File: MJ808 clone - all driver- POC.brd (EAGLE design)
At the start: 35.5 x 35.5 mm, 38 parts, among them IC1 ATTINY4313-MMH, IC2 PRQV8.00CR1510Y00L, IC6 MCP2515, IC7 MAX16820, IC8 MCP2561-2, IC9 TPS709-Q1, K1 CRTL, Q1 PMV213SN,215, X1 22-23-2021, X2 22-23-2021

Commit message: - updated values for LED1 and LED2, re-generated gerbers
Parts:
- LED1: value XMLBWT-00-0000-0000U20E2 -> LTST-C281KRKT
- LED2: value XMLBWT-00-0000-0000U20E2 -> LTST-C281KGKT
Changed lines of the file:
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@@
 <attribute name="VALUE" x="14.405" y="7.885" size="1.27" layer="28" rot="MR270"/>
 </element>
-<element name="LED1" library="led" library_urn="urn:adsk.eagle:library:259" package="CHIP-LED0805" package3d_urn="urn:adsk.eagle:package:15818/1" value="XMLBWT-00-0000-0000U20E2 " x="10.25" y="7.25" smashed="yes">
+<element name="LED1" library="led" library_urn="urn:adsk.eagle:library:259" package="CHIP-LED0805" package3d_urn="urn:adsk.eagle:package:15818/1" value="LTST-C281KRKT" x="10.25" y="7.25" smashed="yes">
 <attribute name="NAME" x="8.75" y="7.25" size="1" layer="25" font="vector" rot="R90" align="center"/>
 <attribute name="VALUE" x="12.79" y="5.98" size="1.27" layer="27" rot="R90"/>
 </element>
-<element name="LED2" library="led" library_urn="urn:adsk.eagle:library:259" package="CHIP-LED0805" package3d_urn="urn:adsk.eagle:package:15818/1" value="XMLBWT-00-0000-0000U20E2 " x="18.75" y="7.25" smashed="yes">
+<element name="LED2" library="led" library_urn="urn:adsk.eagle:library:259" package="CHIP-LED0805" package3d_urn="urn:adsk.eagle:package:15818/1" value="LTST-C281KGKT" x="18.75" y="7.25" smashed="yes">
 <attribute name="NAME" x="20.25" y="7.5" size="1" layer="25" font="vector" rot="R90" align="center"/>
 <attribute name="VALUE" x="21.29" y="5.98" size="1.27" layer="27" rot="R90"/>

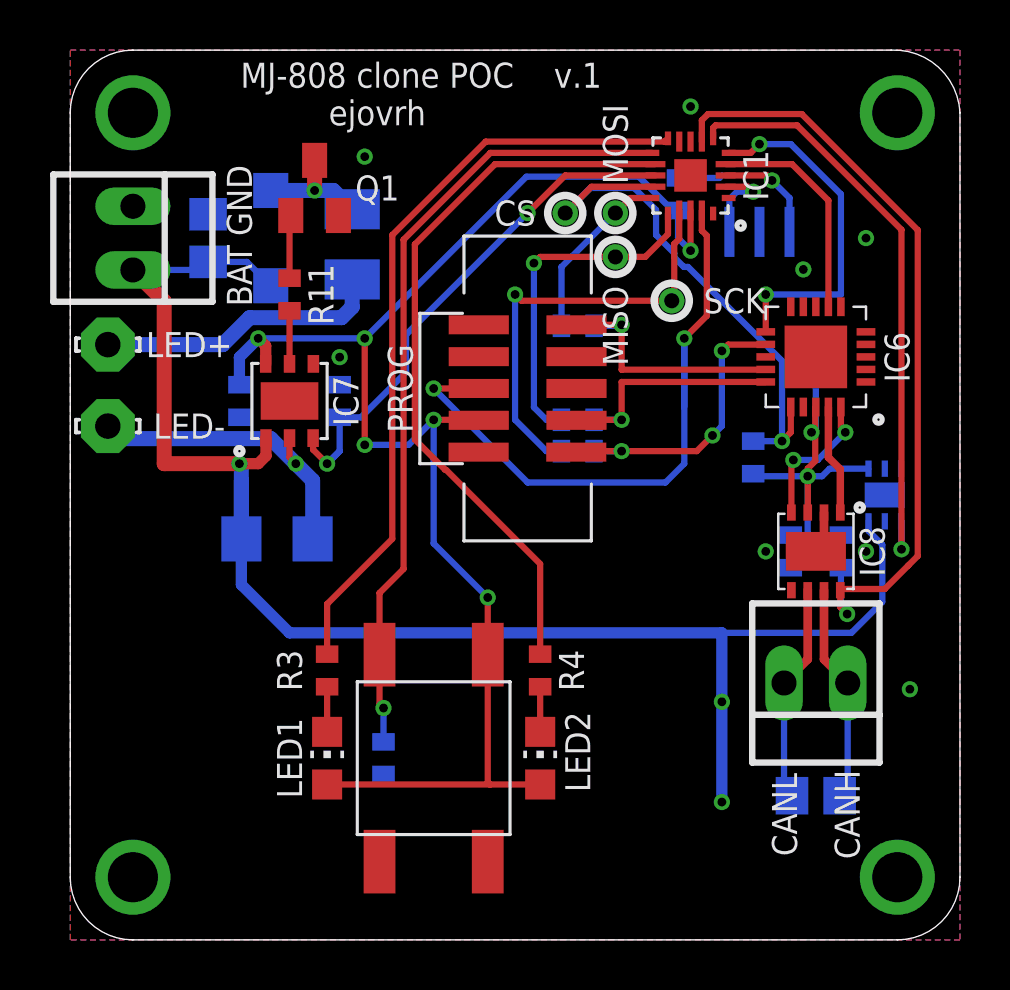
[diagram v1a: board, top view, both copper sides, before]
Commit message: - added copper edge
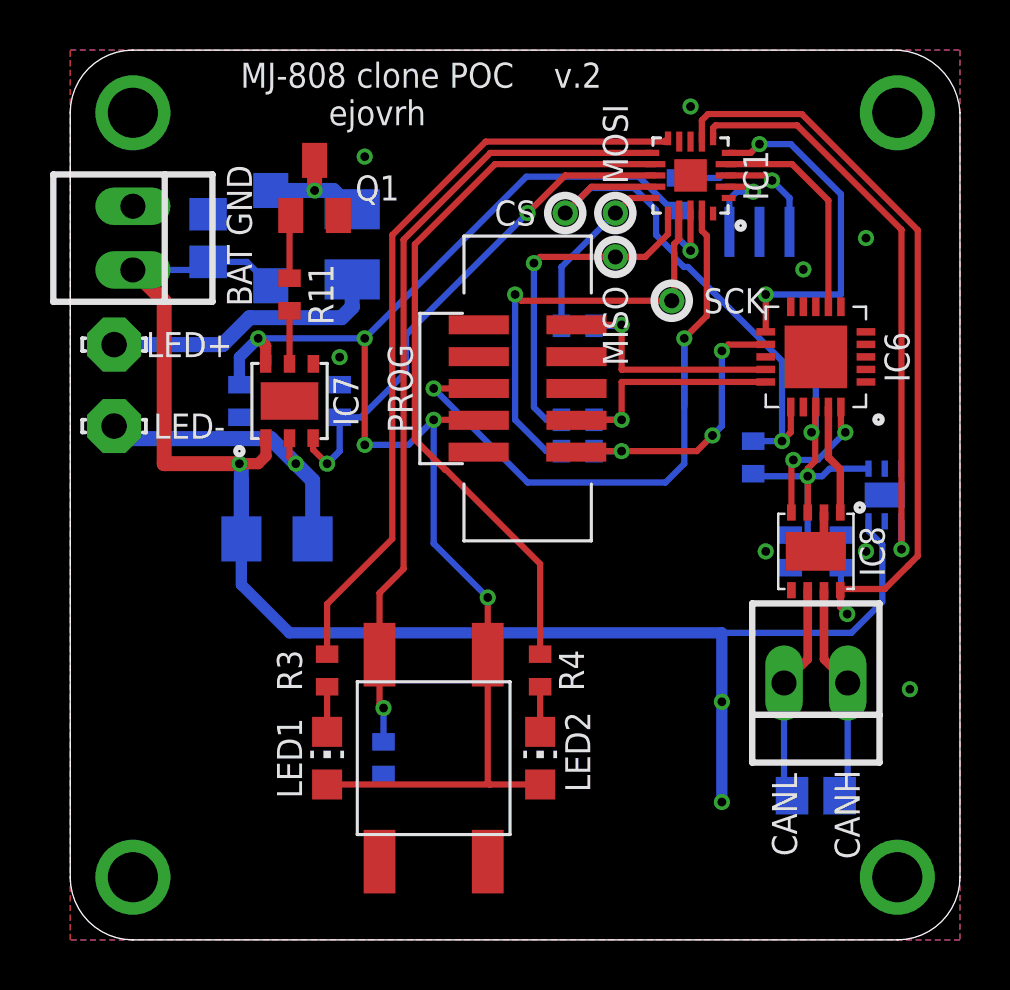
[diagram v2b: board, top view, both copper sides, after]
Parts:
- moved LSP1 0.25 mm to (1.75, 20.5)
- moved LSP2 0.25 mm to (1.75, 23.8)
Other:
- board text added: "v.2"
- board text removed: "v.1"
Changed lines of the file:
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@@
 <?xml version="1.0" encoding="utf-8"?>
 <!DOCTYPE eagle SYSTEM "eagle.dtd">
-<eagle version="8.5.0">
+<eagle version="8.6.1">
 <drawing>
 <settings>
@@
 <wire x1="33" y1="0" x2="35.5" y2="2.5" width="0" layer="20" curve="90"/>
 <wire x1="0" y1="2.5" x2="2.5" y2="0" width="0" layer="20" curve="90"/>
-<text x="20.25" y="34.5" size="1" layer="21" font="vector" align="center">v.1</text>
+<text x="20.25" y="34.5" size="1" layer="21" font="vector" align="center">v.2</text>
 <text x="31" y="5" size="1" layer="25" font="vector" rot="R90" align="center">CANH</text>
 <text x="28.5" y="5" size="1" layer="25" font="vector" rot="R90" align="center">CANL</text>
@@
 </class>
 </classes>
-<designrules name="markovac_2layer *">
+<designrules name="markovac_2layer">
 <description language="hr">&lt;b&gt;EAGLE Design Rules&lt;/b&gt;
 &lt;p&gt;
@@
 <param name="mdViaViaSameLayer" value="8mil"/>
 <param name="mnLayersViaInSmd" value="2"/>
-<param name="mdCopperDimension" value="0mil"/>
+<param name="mdCopperDimension" value="0.5mm"/>
 <param name="mdDrill" value="8mil"/>
 <param name="mdSmdStop" value="0mil"/>
 <param name="msWidth" value="0.2mm"/>
-<param name="msDrill" value="0.3mm"/>
+<param name="msDrill" value="0.35mm"/>
 <param name="msMicroVia" value="0.25mm"/>
 <param name="msBlindViaRatio" value="0.5"/>
@@
 <param name="mlMinCreamFrame" value="0mil"/>
 <param name="mlMaxCreamFrame" value="0mil"/>
-<param name="mlViaStopLimit" value="25mil"/>
+<param name="mlViaStopLimit" value="0.35mm"/>
 <param name="srRoundness" value="0"/>
 <param name="srMinRoundness" value="0mil"/>
@@
 <param name="dpMaxLengthDifference" value="10mm"/>
 <param name="dpGapFactor" value="2.5"/>
-<param name="checkAngle" value="0"/>
-<param name="checkFont" value="1"/>
+<param name="checkAngle" value="1"/>
+<param name="checkFont" value="0"/>
 <param name="checkRestrict" value="1"/>
 <param name="checkStop" value="0"/>
@@
 <attribute name="SPICEPREFIX" value="L" x="11.25" y="27.75" size="1.778" layer="28" rot="MR270" display="off"/>
 </element>
-<element name="LSP1" library="solpad" library_urn="urn:adsk.eagle:library:364" package="LSP10" package3d_urn="urn:adsk.eagle:package:26501/1" value="LSP10" x="1.5" y="20.5" smashed="yes">
-<attribute name="VALUE" x="1.5" y="20.754" size="0.0254" layer="27"/>
-</element>
-<element name="LSP2" library="solpad" library_urn="urn:adsk.eagle:library:364" package="LSP10" package3d_urn="urn:adsk.eagle:package:26501/1" value="LSP10" x="1.5" y="23.75" smashed="yes">
-<attribute name="VALUE" x="1.5" y="24.004" size="0.0254" layer="27"/>
+<element name="LSP1" library="solpad" library_urn="urn:adsk.eagle:library:364" package="LSP10" package3d_urn="urn:adsk.eagle:package:26501/1" value="LSP10" x="1.75" y="20.5" smashed="yes">
+<attribute name="VALUE" x="1.75" y="20.754" size="0.0254" layer="27"/>
+</element>
+<element name="LSP2" library="solpad" library_urn="urn:adsk.eagle:library:364" package="LSP10" package3d_urn="urn:adsk.eagle:package:26501/1" value="LSP10" x="1.75" y="23.75" smashed="yes">
+<attribute name="VALUE" x="1.75" y="24.004" size="0.0254" layer="27"/>
 </element>
 <element name="Q1" library="adafruit" library_urn="urn:adsk.eagle:library:420" package="SOT23" value="PMV213SN,215" x="9.75" y="30" smashed="yes">
@@
 <via x="9" y="19" extent="1-16" drill="0.35"/>
 <wire x1="8" y1="20" x2="9" y2="19" width="0.6" layer="16"/>
-<wire x1="1.5" y1="20.5" x2="2" y2="20" width="0.6" layer="16"/>
-<wire x1="2" y1="20" x2="8" y2="20" width="0.6" layer="16"/>
+<wire x1="1.75" y1="20.5" x2="2.25" y2="20" width="0.6" layer="16"/>
+<wire x1="2.25" y1="20" x2="8" y2="20" width="0.6" layer="16"/>
 <wire x1="9" y1="19" x2="9.672" y2="18.328" width="0.6" layer="16"/>
 <wire x1="9.672" y1="18.328" x2="9.672" y2="16" width="0.6" layer="16"/>
@@
 <contactref element="L1" pad="2"/>
 <contactref element="LSP2" pad="MP"/>
-<wire x1="1.5" y1="23.75" x2="6.08326875" y2="23.75" width="0.6" layer="16"/>
+<wire x1="1.75" y1="23.75" x2="6.08326875" y2="23.75" width="0.6" layer="16"/>
 <wire x1="6.08326875" y1="23.75" x2="7.15826875" y2="24.825" width="0.6" layer="16"/>
 <wire x1="10.825" y1="24.825" x2="7.15826875" y2="24.825" width="0.6" layer="16"/>

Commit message: - sized down ground plane of ICs to make soldering easier - corrected tname and bname positions
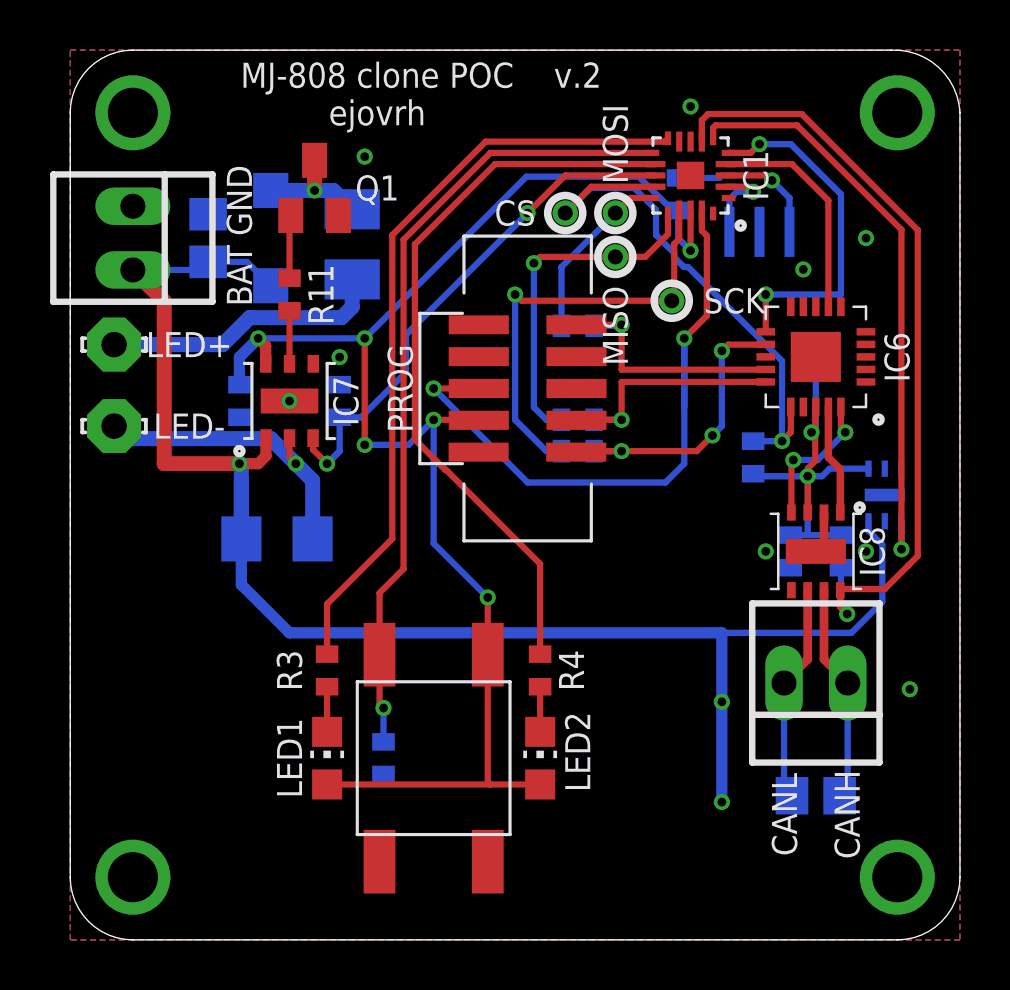
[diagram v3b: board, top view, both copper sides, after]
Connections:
- net GND: no longer IC6.GND1
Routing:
- net GND: vias 12 -> 13
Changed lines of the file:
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@@
 <grid distance="0.25" unitdist="mm" unit="mm" style="dots" multiple="1" display="yes" altdistance="0.01" altunitdist="mm" altunit="mm"/>
 <layers>
-<layer number="1" name="Top" color="4" fill="1" visible="yes" active="yes"/>
+<layer number="1" name="Top" color="4" fill="1" visible="no" active="yes"/>
 <layer number="2" name="Route2" color="1" fill="3" visible="no" active="no"/>
 <layer number="3" name="Route3" color="4" fill="3" visible="no" active="no"/>
@@
 <layer number="19" name="Unrouted" color="6" fill="1" visible="yes" active="yes"/>
 <layer number="20" name="Dimension" color="24" fill="1" visible="yes" active="yes"/>
-<layer number="21" name="tPlace" color="7" fill="1" visible="yes" active="yes"/>
+<layer number="21" name="tPlace" color="7" fill="1" visible="no" active="yes"/>
 <layer number="22" name="bPlace" color="7" fill="1" visible="yes" active="yes"/>
-<layer number="23" name="tOrigins" color="15" fill="1" visible="yes" active="yes"/>
+<layer number="23" name="tOrigins" color="15" fill="1" visible="no" active="yes"/>
 <layer number="24" name="bOrigins" color="15" fill="1" visible="yes" active="yes"/>
 <layer number="25" name="tNames" color="7" fill="1" visible="no" active="yes"/>
-<layer number="26" name="bNames" color="7" fill="1" visible="no" active="yes"/>
+<layer number="26" name="bNames" color="7" fill="1" visible="yes" active="yes"/>
 <layer number="27" name="tValues" color="7" fill="1" visible="no" active="yes"/>
 <layer number="28" name="bValues" color="7" fill="1" visible="no" active="yes"/>
@@
 <layer number="37" name="tTest" color="7" fill="1" visible="no" active="yes"/>
 <layer number="38" name="bTest" color="7" fill="1" visible="no" active="yes"/>
-<layer number="39" name="tKeepout" color="4" fill="11" visible="yes" active="yes"/>
+<layer number="39" name="tKeepout" color="4" fill="11" visible="no" active="yes"/>
 <layer number="40" name="bKeepout" color="1" fill="11" visible="yes" active="yes"/>
-<layer number="41" name="tRestrict" color="4" fill="10" visible="yes" active="yes"/>
+<layer number="41" name="tRestrict" color="4" fill="10" visible="no" active="yes"/>
 <layer number="42" name="bRestrict" color="1" fill="10" visible="yes" active="yes"/>
-<layer number="43" name="vRestrict" color="2" fill="10" visible="yes" active="yes"/>
+<layer number="43" name="vRestrict" color="2" fill="10" visible="no" active="yes"/>
 <layer number="44" name="Drills" color="7" fill="1" visible="yes" active="yes"/>
 <layer number="45" name="Holes" color="7" fill="1" visible="yes" active="yes"/>
@@
 <layer number="49" name="Reference" color="7" fill="1" visible="no" active="yes"/>
 <layer number="50" name="dxf" color="7" fill="1" visible="no" active="no"/>
-<layer number="51" name="tDocu" color="7" fill="1" visible="yes" active="yes"/>
+<layer number="51" name="tDocu" color="7" fill="1" visible="no" active="yes"/>
 <layer number="52" name="bDocu" color="7" fill="1" visible="yes" active="yes"/>
 <layer number="53" name="tGND_GNDA" color="7" fill="9" visible="no" active="no"/>
@@
 </element>
 <element name="R10" library="rcl" library_urn="urn:adsk.eagle:library:334" package="R1206" package3d_urn="urn:adsk.eagle:package:23540/2" value="0.25 / 2W" x="8.25" y="16" smashed="yes" rot="MR0">
-<attribute name="NAME" x="8.25" y="13" size="1" layer="26" font="vector" rot="MR0" align="center"/>
+<attribute name="NAME" x="8.25" y="14.25" size="1" layer="26" font="vector" rot="MR0" align="center"/>
 <attribute name="VALUE" x="8.885" y="13.46" size="1.27" layer="28" rot="MR0"/>
 </element>
@@
 </element>
 <element name="IC2" library="PRQV8.00CR1510Y00L - 8MHz resonator" package="SMT" value=" PRQV8.00CR1510Y00L" x="27.5" y="28.25" smashed="yes" rot="MR0">
-<attribute name="NAME" x="30.45" y="28.25" size="1" layer="26" font="vector" rot="MR90" align="center"/>
+<attribute name="NAME" x="30.2" y="28.25" size="1" layer="26" font="vector" rot="MR90" align="center"/>
 </element>
 <element name="PROG" library="SPI 1.27mm 10pin header" package="SMT-JTAG" value="SPI-1.27-10-PIN-HEADER" x="18.25" y="22" smashed="yes" rot="R90">
@@
 </element>
 <element name="R9" library="rcl" library_urn="urn:adsk.eagle:library:334" package="R0402" package3d_urn="urn:adsk.eagle:package:23547/1" value="330" x="20.25" y="20.75" smashed="yes" rot="MR0">
-<attribute name="NAME" x="20.25" y="24.5" size="1" layer="26" font="vector" rot="MR0" align="center"/>
+<attribute name="NAME" x="20.25" y="22" size="1" layer="26" font="vector" rot="MR0" align="center"/>
 <attribute name="VALUE" x="20.885" y="18.845" size="1.27" layer="28" rot="MR0"/>
 </element>
 <element name="R8" library="rcl" library_urn="urn:adsk.eagle:library:334" package="R0402" package3d_urn="urn:adsk.eagle:package:23547/1" value="330" x="20.25" y="24.5" smashed="yes" rot="MR0">
-<attribute name="NAME" x="20.25" y="28.25" size="1" layer="26" font="vector" rot="MR0" align="center"/>
+<attribute name="NAME" x="20.25" y="25.75" size="1" layer="26" font="vector" rot="MR0" align="center"/>
 <attribute name="VALUE" x="20.885" y="22.595" size="1.27" layer="28" rot="MR0"/>
 </element>
 <element name="R6" library="rcl" library_urn="urn:adsk.eagle:library:334" package="R0402" package3d_urn="urn:adsk.eagle:package:23547/1" value="330" x="20.25" y="19.5" smashed="yes" rot="MR0">
-<attribute name="NAME" x="20.25" y="23.25" size="1" layer="26" font="vector" rot="MR0" align="center"/>
+<attribute name="NAME" x="20.25" y="18.25" size="1" layer="26" font="vector" rot="MR0" align="center"/>
 <attribute name="VALUE" x="20.885" y="17.595" size="1.27" layer="28" rot="MR0"/>
 </element>
 <element name="R12" library="rcl" library_urn="urn:adsk.eagle:library:334" package="R0402" package3d_urn="urn:adsk.eagle:package:23547/1" value="10k" x="30.75" y="15.5" smashed="yes" rot="MR270">
-<attribute name="NAME" x="32" y="15.5" size="1" layer="26" rot="MR270" align="center"/>
+<attribute name="NAME" x="32" y="13.25" size="1" layer="26" rot="MR270" align="center"/>
 <attribute name="VALUE" x="32.655" y="16.135" size="1.27" layer="28" rot="MR270"/>
 </element>
@@
 <contactref element="Q1" pad="2"/>
 <contactref element="IC6" pad="GND"/>
-<contactref element="IC6" pad="GND1"/>
 <contactref element="IC6" pad="GND6"/>
 <contactref element="IC8" pad="GND"/>
@@
 <wire x1="25.9" y1="30.4" x2="26" y2="30.5" width="0.25" layer="16"/>
 <contactref element="R1" pad="2"/>
+<via x="8.75" y="21.5" extent="1-16" drill="0.35"/>
+<wire x1="29.75" y1="23.9" x2="29.75" y2="23.26" width="0" layer="19" extent="1-16"/>
+<wire x1="29.75" y1="15.5" x2="28.75" y2="14.85" width="0" layer="19" extent="1-16"/>
 </signal>
 <signal name="DIM_FRONT">

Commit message: - added pulldown on 5V LDO enable pin
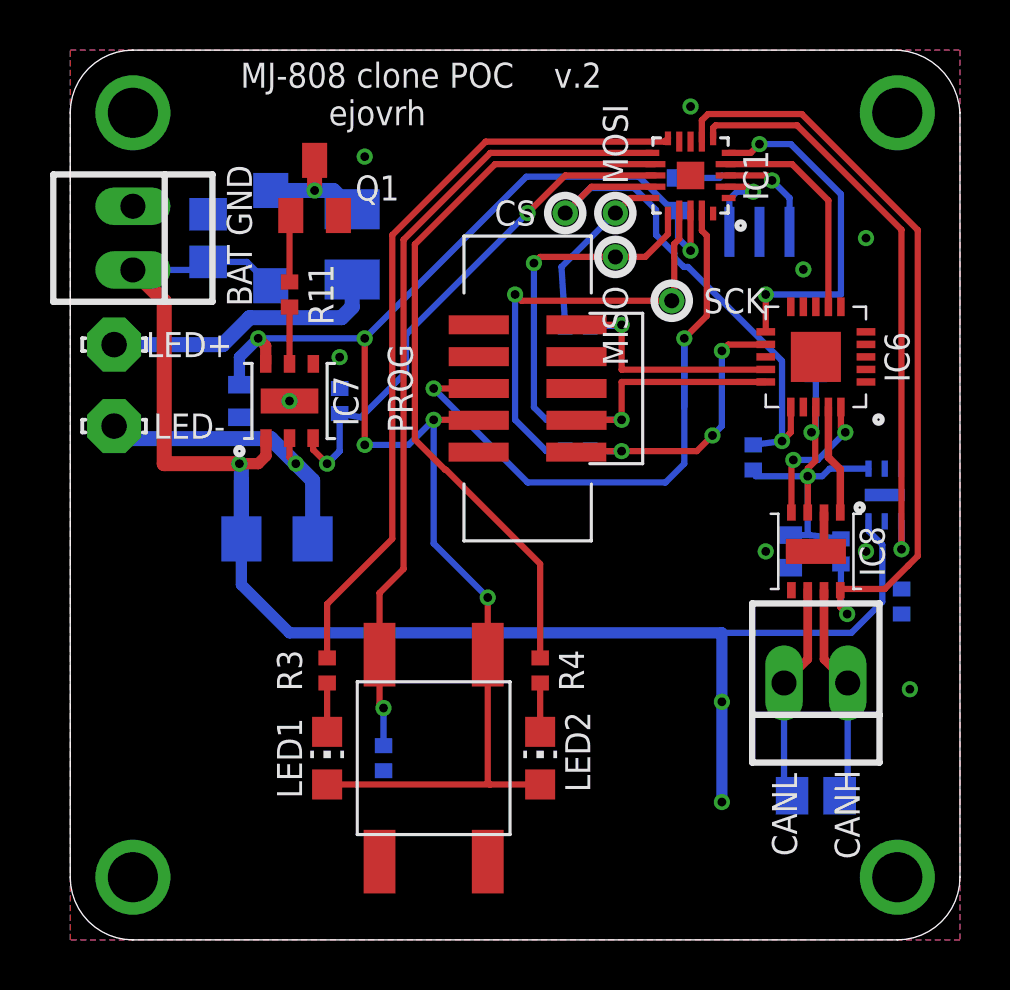
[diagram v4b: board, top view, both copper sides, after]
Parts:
- added R5: 10k, rcl:R0402
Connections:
- net EN: now also R5.2
- net GND: now also R5.1
